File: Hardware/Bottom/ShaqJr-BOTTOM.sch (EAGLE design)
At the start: 35 parts

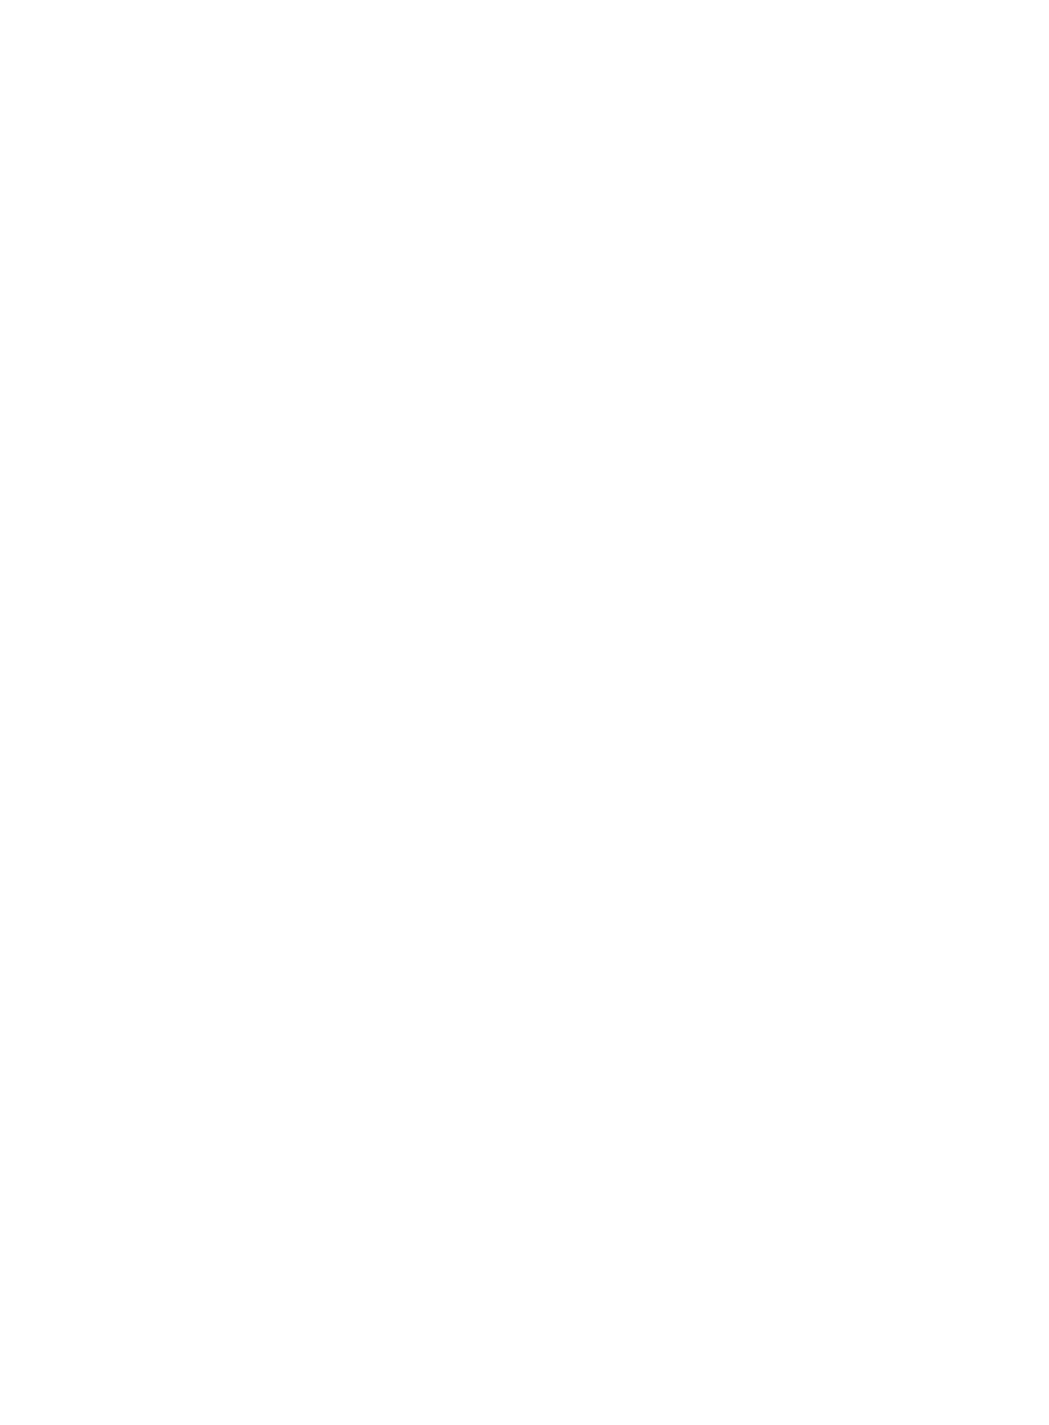
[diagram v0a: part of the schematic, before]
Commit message: completed take 007, may need to review polygons- gnd and 3.3v
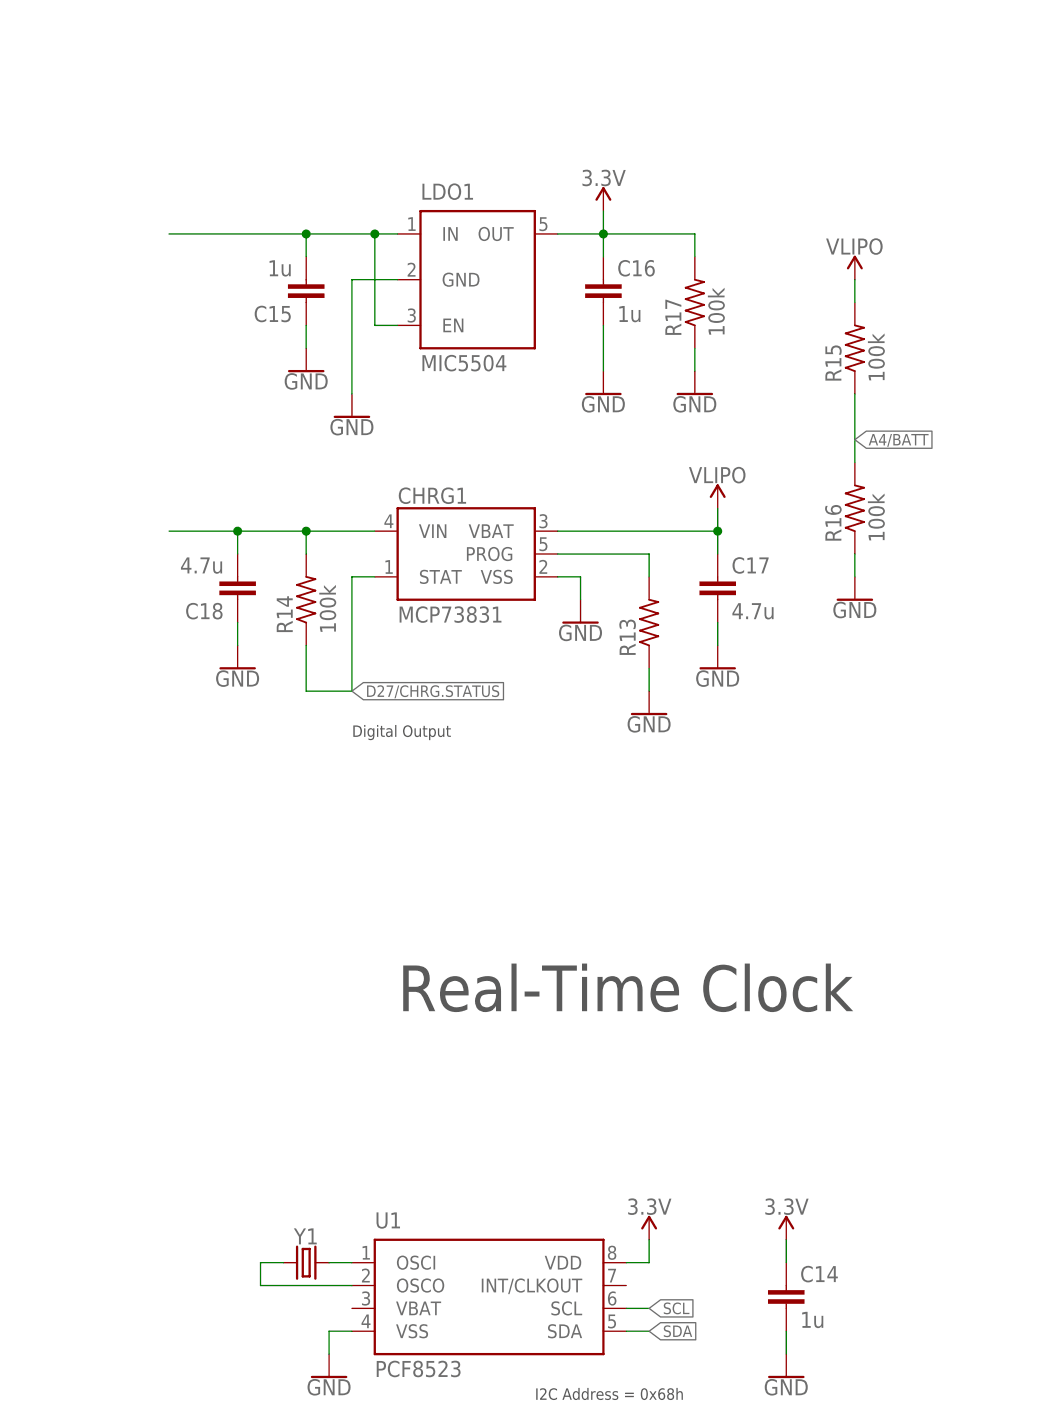
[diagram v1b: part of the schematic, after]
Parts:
- added C14, C15, C16: 1u, LinnesLab-Passives:CAPACITOR0603
- added C17, C18: 4.7u, LinnesLab-Passives:CAPACITOR0603
- added CHRG1: MCP73831, LinnesLab-Power:MCP73831
- added LDO1: MIC5504, LinnesLab-Power:MIC5504
- added R13: (no value), LinnesLab-Passives:RESISTOR0603
- added R14, R15, R16, R17: 100k, LinnesLab-Passives:RESISTOR0603
- added U1: PCF8523, LinnesLab-Clocks:PCF8523
- added Y1: 32.7680kHz, LinnesLab-Clocks:CRYSTALECS-.327-12.5-12-C-TR
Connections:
- new net A4/BATT: R15.1, R16.2
- new net D27/CHRG.STATUS: CHRG1.STAT, R14.1
- new net N$10: U1.OSCI, Y1.2
- new net N$17: CHRG1.PROG, R13.2
- new net N$9: U1.OSCO, Y1.1
- new net VIN1: C15.2, C18.2, CHRG1.VIN, LDO1.EN, LDO1.IN, R14.2
- new net VLIPO: C17.1, CHRG1.VBAT, R15.2
- net 3.3V: now also C14.1, C16.1, LDO1.OUT, R17.2, U1.VDD
- net GND: now also C14.2, C15.1, C16.2, C17.2, C18.1, CHRG1.VSS, LDO1.GND, R13.1, R16.1, R17.1, U1.VSS
- net SCL: now also U1.SCL
- net SDA: now also U1.SDA
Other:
- note added: "Digital Output"
- note added: "I2C Address = 0x68h"
- note added: "Real-Time Clock"

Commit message: Finished Take 008
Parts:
- removed C15, C16: 1u, LinnesLab-Passives:CAPACITOR0603
- removed C17, C18: 4.7u, LinnesLab-Passives:CAPACITOR0603
- removed CHRG1: MCP73831, LinnesLab-Power:MCP73831
- removed LDO1: MIC5504, LinnesLab-Power:MIC5504
- removed R13: (no value), LinnesLab-Passives:RESISTOR0603
- removed R14, R15, R16, R17: 100k, LinnesLab-Passives:RESISTOR0603
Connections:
- net A6/TIA renamed A5/TIA
- net A7/PPG renamed A4/PPG
- net D29/LED.CTRL renamed D30/LED.CTRL
- removed net A4/BATT: R15.1, R16.2
- removed net D27/CHRG.STATUS: CHRG1.STAT, R14.1
- removed net N$17: CHRG1.PROG, R13.2
- removed net VIN1: C15.2, C18.2, CHRG1.VIN, LDO1.EN, LDO1.IN, R14.2
- removed net VLIPO: C17.1, CHRG1.VBAT, R15.2
- net 3.3V: no longer C16.1, LDO1.OUT, R17.2
- net GND: no longer C15.1, C16.2, C17.2, C18.1, CHRG1.VSS, LDO1.GND, R13.1, R16.1, R17.1
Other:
- note removed: "Digital Output"
- moved on the sheet: C14, U1, Y1

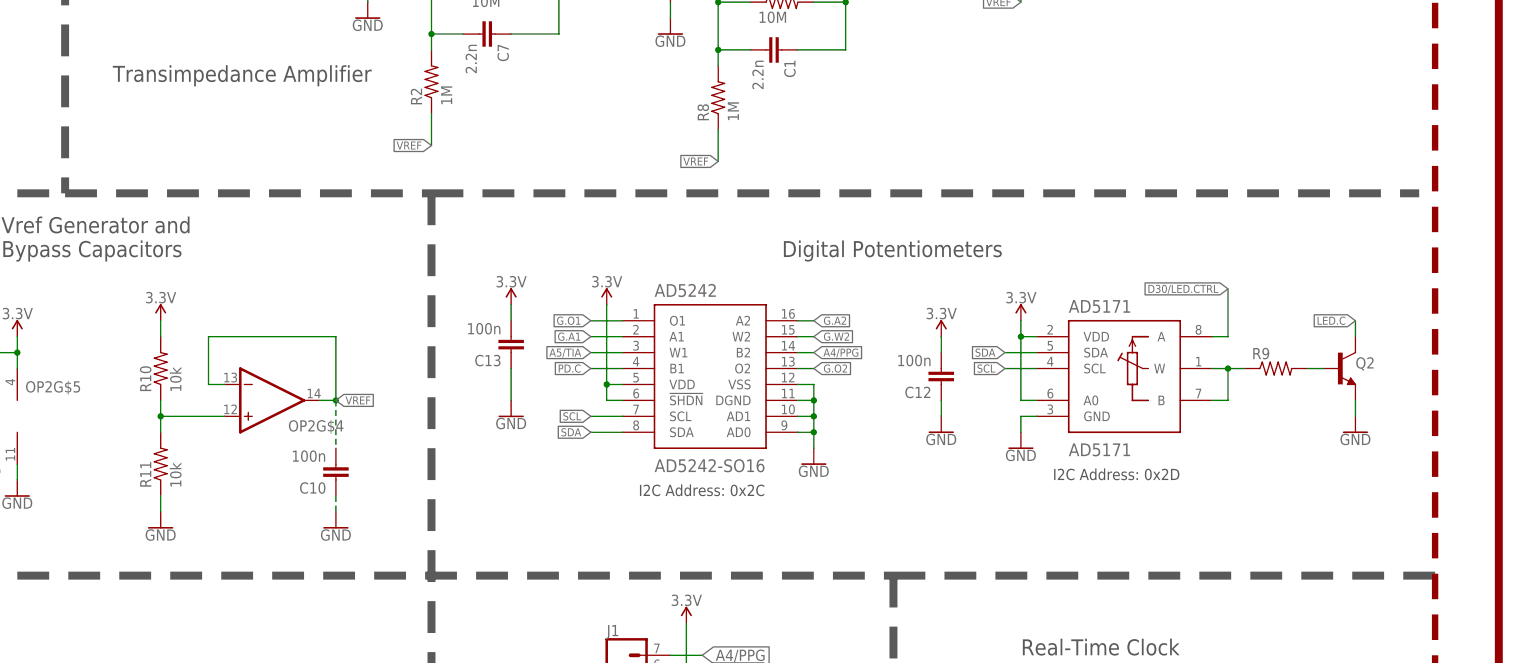
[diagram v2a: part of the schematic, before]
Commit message: Added ppg module brd, sch and bom, and ex ino code
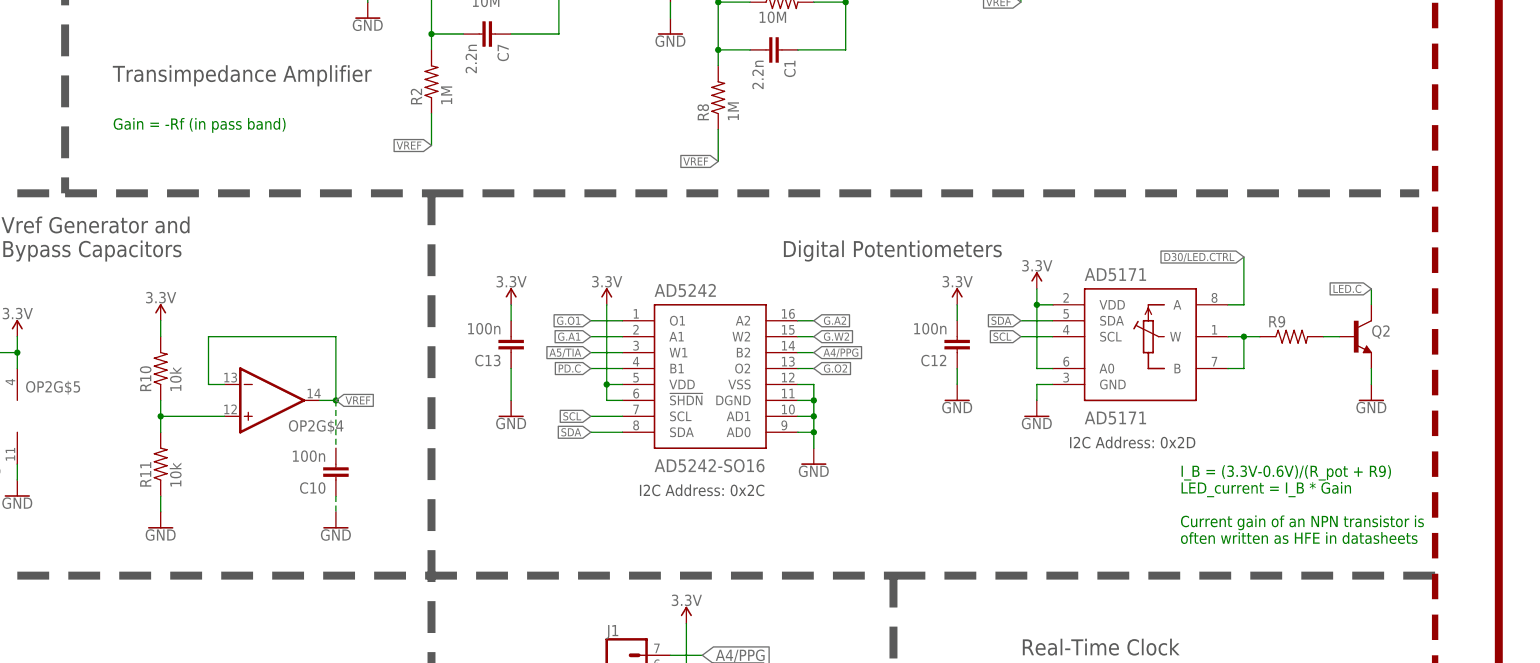
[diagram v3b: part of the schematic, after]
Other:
- note added: "Gain = -Rf (in pass band)"
- note added: "I_B = (3.3V-0.6V)/(R_pot + R9) LED_current = I_B * Gain Current gain of an NPN transistor is often written as HFE in datasheets"
- moved on the sheet: AD5171, C12, Q2, R9
